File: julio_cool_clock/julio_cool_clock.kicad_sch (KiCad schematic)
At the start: 19 parts, among them J1 PJ-102AH, J2 Conn_01x06, Y1 Crystal_16MHz

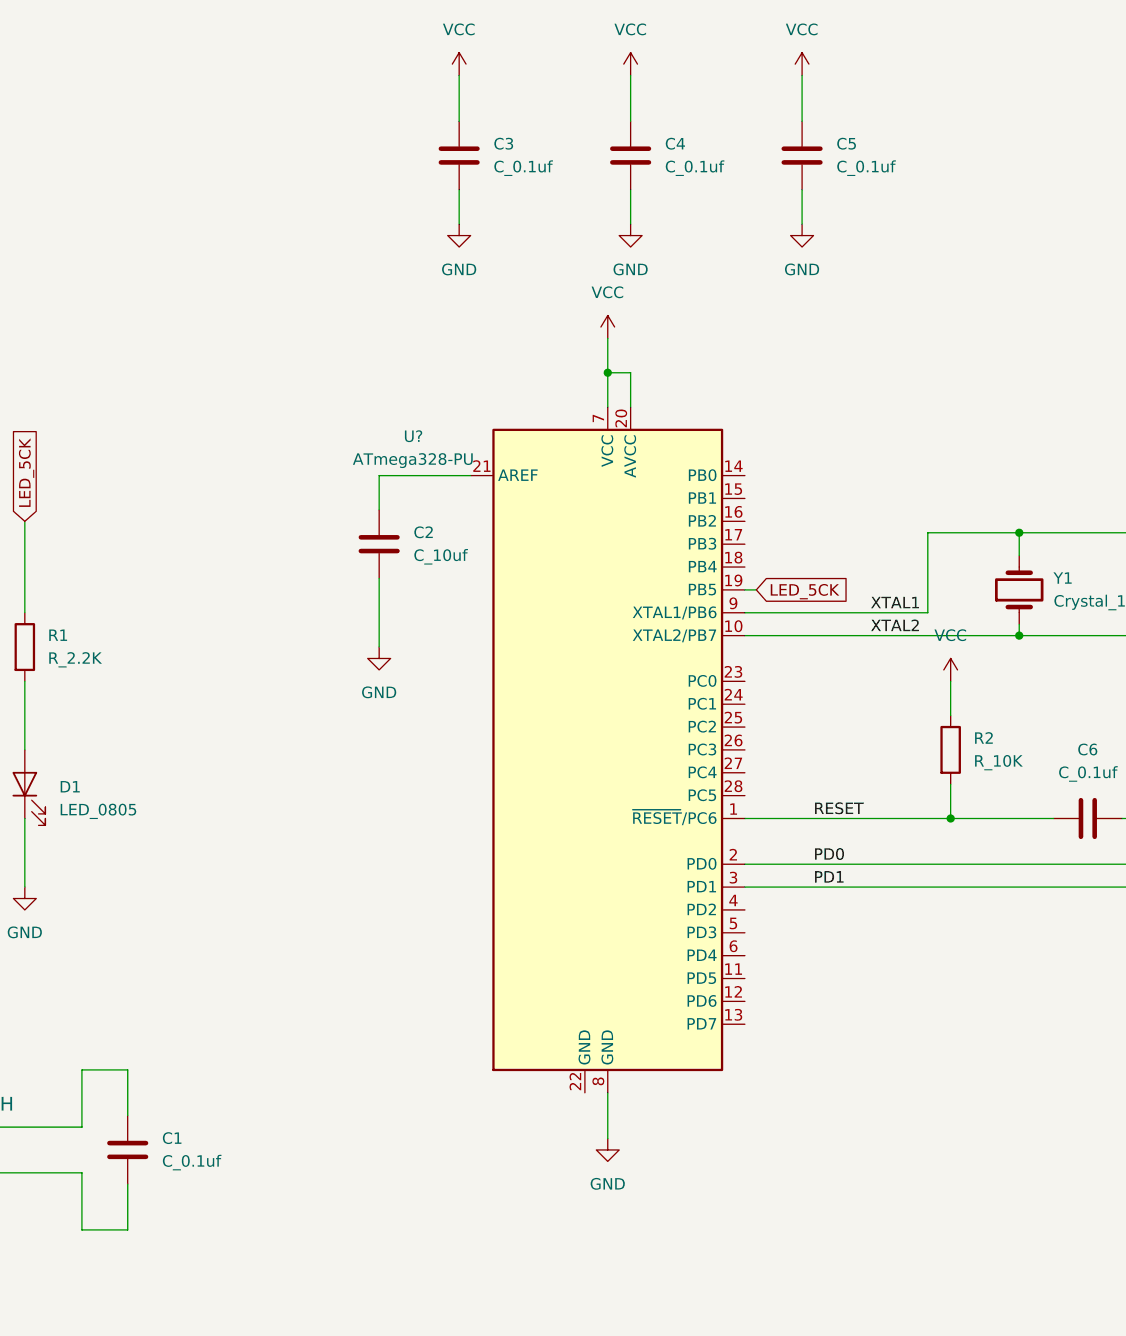
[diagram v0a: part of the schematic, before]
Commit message: Design Commit 1.1
Adjusted the starting schematic with 10uF capacitors in place of the polar capacitors in the lecture slide.
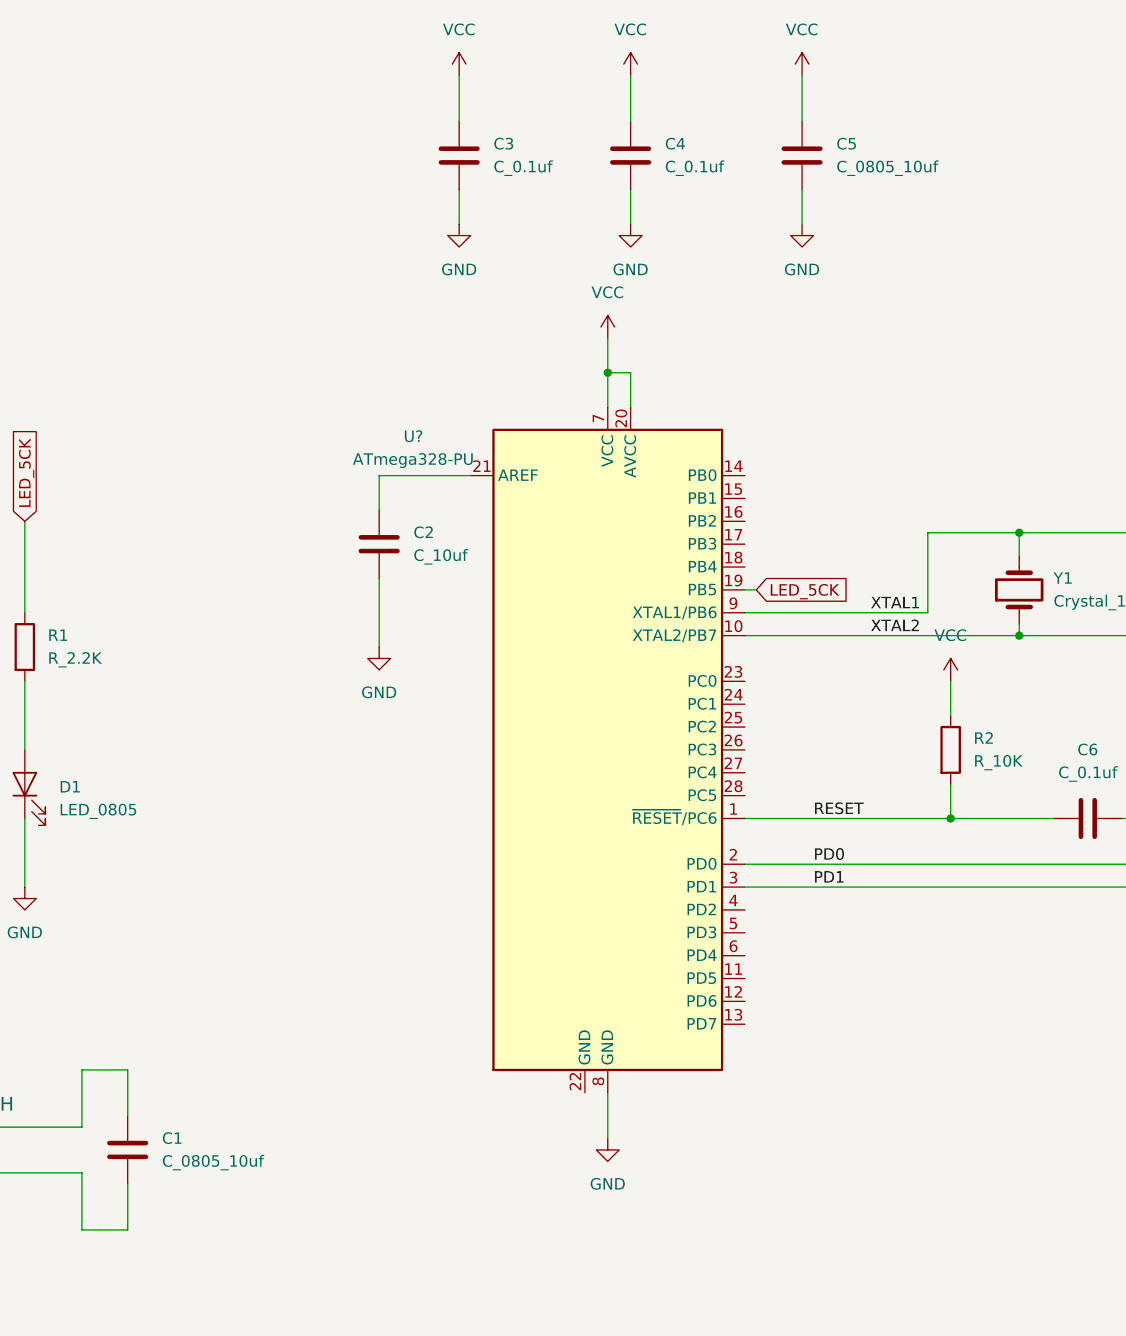
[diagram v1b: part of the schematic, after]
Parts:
- removed C1, C5: C_0.1uf, footprints:C_0805_2012Metric, symbol HPS:C_0805_0.1uf
- added C1, C5: C_0805_10uf, footprints:C_0805_2012Metric, symbol HPS:C_0805_10uf
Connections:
- net GND: now also C5.2
- net VCC: now also C5.1
- net at J1.1 (POLE): now also C1.1
- net at J1.2 (OUT): now also C1.2
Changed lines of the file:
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@@
+    (pin "2")
+  )
+  (symbol (lib_id "HPS:C_0805_10uf") (at 90.17 138.43 0) (unit 1)
+    (in_bom yes) (on_board yes) (fields_autoplaced)
+    (property "Reference" "C1" (id 0) (at 93.98 137.1599 0)
+      (effects (font (size 1.27 1.27)) (justify left))
+    )
+    (property "Value" "C_0805_10uf" (id 1) (at 93.98 139.6999 0)
+      (effects (font (size 1.27 1.27)) (justify left))
+    )
+    (property "Footprint" "footprints:C_0805_2012Metric" (id 2) (at 91.1352 142.24 0)
+      (effects (font (size 1.27 1.27)) hide)
+    )
+    (property "Datasheet" "https://search.murata.co.jp/Ceramy/image/img/A01X/G101/ENG/GRM21BR61E106KA73-01.pdf" (id 3) (at 90.805 135.89 0)
+      (effects (font (size 1.27 1.27)) hide)
+    )
+    (property "MFG" "Murata Electronics" (id 4) (at 90.17 144.78 0)
+      (effects (font (size 1.27 1.27)) hide)
+    )
+    (property "MPN" "GRM21BR61E106KA73L" (id 5) (at 90.17 147.32 0)
+      (effects (font (size 1.27 1.27)) hide)
+    )
+    (property "Digikey PN" "490-5523-1-ND" (id 6) (at 90.17 152.4 0)
+      (effects (font (size 1.27 1.27)) hide)
+    )
+    (property "Mouser PN" "N/A" (id 7) (at 90.17 154.94 0)
+      (effects (font (size 1.27 1.27)) hide)
+    )
+    (property "Voltage" "N/A" (id 8) (at 90.17 157.48 0)
+      (effects (font (size 1.27 1.27)) hide)
+    )
+    (property "Dielectric" "N/A" (id 9) (at 90.17 157.48 0)
+      (effects (font (size 1.27 1.27)) hide)
+    )
+    (property "Tolerance" "N/A" (id 10) (at 90.17 157.48 0)
+      (effects (font (size 1.27 1.27)) hide)
+    )
+    (pin "1")
     (pin "2")
   )
@@
     )
     (pin "1")
-  )
-  (symbol (lib_id "HPS:C_0805_0.1uf") (at 90.17 138.43 0) (unit 1)
-    (in_bom yes) (on_board yes) (fields_autoplaced)
-    (property "Reference" "C1" (id 0) (at 93.98 137.1599 0)
-      (effects (font (size 1.27 1.27)) (justify left))
-    )
-    (property "Value" "C_0.1uf" (id 1) (at 93.98 139.6999 0)
-      (effects (font (size 1.27 1.27)) (justify left))
-    )
-    (property "Footprint" "footprints:C_0805_2012Metric" (id 2) (at 91.1352 142.24 0)
-      (effects (font (size 1.27 1.27)) hide)
-    )
-    (property "Datasheet" "https://datasheets.avx.com/X7RDielectric.pdf" (id 3) (at 90.805 135.89 0)
-      (effects (font (size 1.27 1.27)) hide)
-    )
-    (property "MFG" "AVX Corporation" (id 4) (at 90.17 144.78 0)
-      (effects (font (size 1.27 1.27)) hide)
-    )
-    (property "MPN" "08055C104KAT2A" (id 5) (at 90.17 147.32 0)
-      (effects (font (size 1.27 1.27)) hide)
-    )
-    (property "Digikey PN" "478-1395-1-ND" (id 6) (at 90.17 152.4 0)
-      (effects (font (size 1.27 1.27)) hide)
-    )
-    (property "Mouser PN" "N/A" (id 7) (at 90.17 154.94 0)
-      (effects (font (size 1.27 1.27)) hide)
-    )
-    (property "Voltage" "N/A" (id 8) (at 90.17 157.48 0)
-      (effects (font (size 1.27 1.27)) hide)
-    )
-    (property "Dielectric" "N/A" (id 9) (at 90.17 157.48 0)
-      (effects (font (size 1.27 1.27)) hide)
-    )
-    (property "Tolerance" "N/A" (id 10) (at 90.17 157.48 0)
-      (effects (font (size 1.27 1.27)) hide)
-    )
-    (pin "1")
-    (pin "2")
   )
   (symbol (lib_id "HPS:VCC") (at 165.1 19.05 0) (unit 1)
@@
     (pin "2")
   )
-  (symbol (lib_id "HPS:C_0805_0.1uf") (at 165.1 27.94 0) (unit 1)
+  (symbol (lib_id "HPS:C_0805_10uf") (at 165.1 27.94 0) (unit 1)
     (in_bom yes) (on_board yes) (fields_autoplaced)
     (property "Reference" "C5" (id 0) (at 168.91 26.6699 0)
       (effects (font (size 1.27 1.27)) (justify left))
     )
-    (property "Value" "C_0.1uf" (id 1) (at 168.91 29.2099 0)
+    (property "Value" "C_0805_10uf" (id 1) (at 168.91 29.2099 0)
       (effects (font (size 1.27 1.27)) (justify left))
     )
@@
       (effects (font (size 1.27 1.27)) hide)
     )
-    (property "Datasheet" "https://datasheets.avx.com/X7RDielectric.pdf" (id 3) (at 165.735 25.4 0)
-      (effects (font (size 1.27 1.27)) hide)
-    )
-    (property "MFG" "AVX Corporation" (id 4) (at 165.1 34.29 0)
-      (effects (font (size 1.27 1.27)) hide)
-    )
-    (property "MPN" "08055C104KAT2A" (id 5) (at 165.1 36.83 0)
-      (effects (font (size 1.27 1.27)) hide)
-    )
-    (property "Digikey PN" "478-1395-1-ND" (id 6) (at 165.1 41.91 0)
+    (property "Datasheet" "https://search.murata.co.jp/Ceramy/image/img/A01X/G101/ENG/GRM21BR61E106KA73-01.pdf" (id 3) (at 165.735 25.4 0)
+      (effects (font (size 1.27 1.27)) hide)
+    )
+    (property "MFG" "Murata Electronics" (id 4) (at 165.1 34.29 0)
+      (effects (font (size 1.27 1.27)) hide)
+    )
+    (property "MPN" "GRM21BR61E106KA73L" (id 5) (at 165.1 36.83 0)
+      (effects (font (size 1.27 1.27)) hide)
+    )
+    (property "Digikey PN" "490-5523-1-ND" (id 6) (at 165.1 41.91 0)
       (effects (font (size 1.27 1.27)) hide)
     )
@@
       (reference "#PWR?") (unit 1) (value "GND") (footprint "")
     )
-    (path "/862e7416-362f-490f-9b26-7a6c1e75c0c9"
-      (reference "C1") (unit 1) (value "C_0.1uf") (footprint "footprints:C_0805_2012Metric")
+    (path "/6f97759c-1ad8-4f0e-a04e-d2e50a497ce6"
+      (reference "C1") (unit 1) (value "C_0805_10uf") (footprint "footprints:C_0805_2012Metric")
     )
     (path "/d1f31220-e097-488d-9540-ed62728793d1"
@@
       (reference "C4") (unit 1) (value "C_0.1uf") (footprint "footprints:C_0805_2012Metric")
     )
-    (path "/e1700882-ee6c-4685-9457-9c368506616a"
-      (reference "C5") (unit 1) (value "C_0.1uf") (footprint "footprints:C_0805_2012Metric")
+    (path "/efddba53-3b77-46b4-8321-0aff9be2da48"
+      (reference "C5") (unit 1) (value "C_0805_10uf") (footprint "footprints:C_0805_2012Metric")
     )
     (path "/2f4099bf-4d54-4041-920b-635ae3bcc86c"

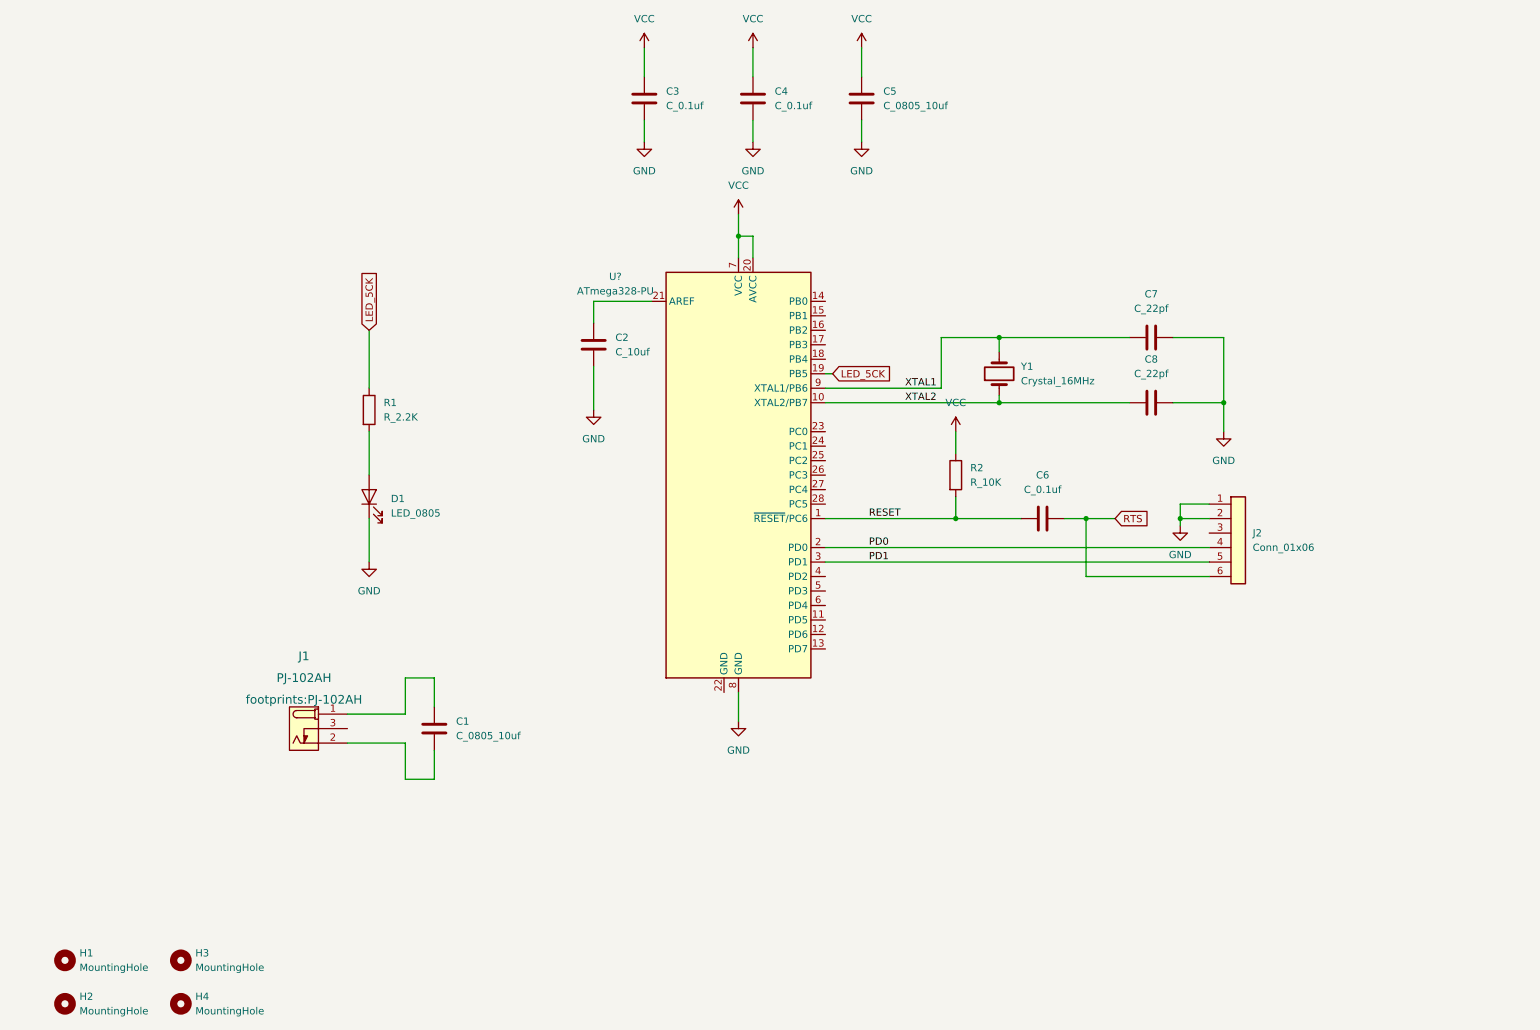
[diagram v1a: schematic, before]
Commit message: Design Commit 2
In this commit, I adjusted the MCU schematic section and added the power input portion.
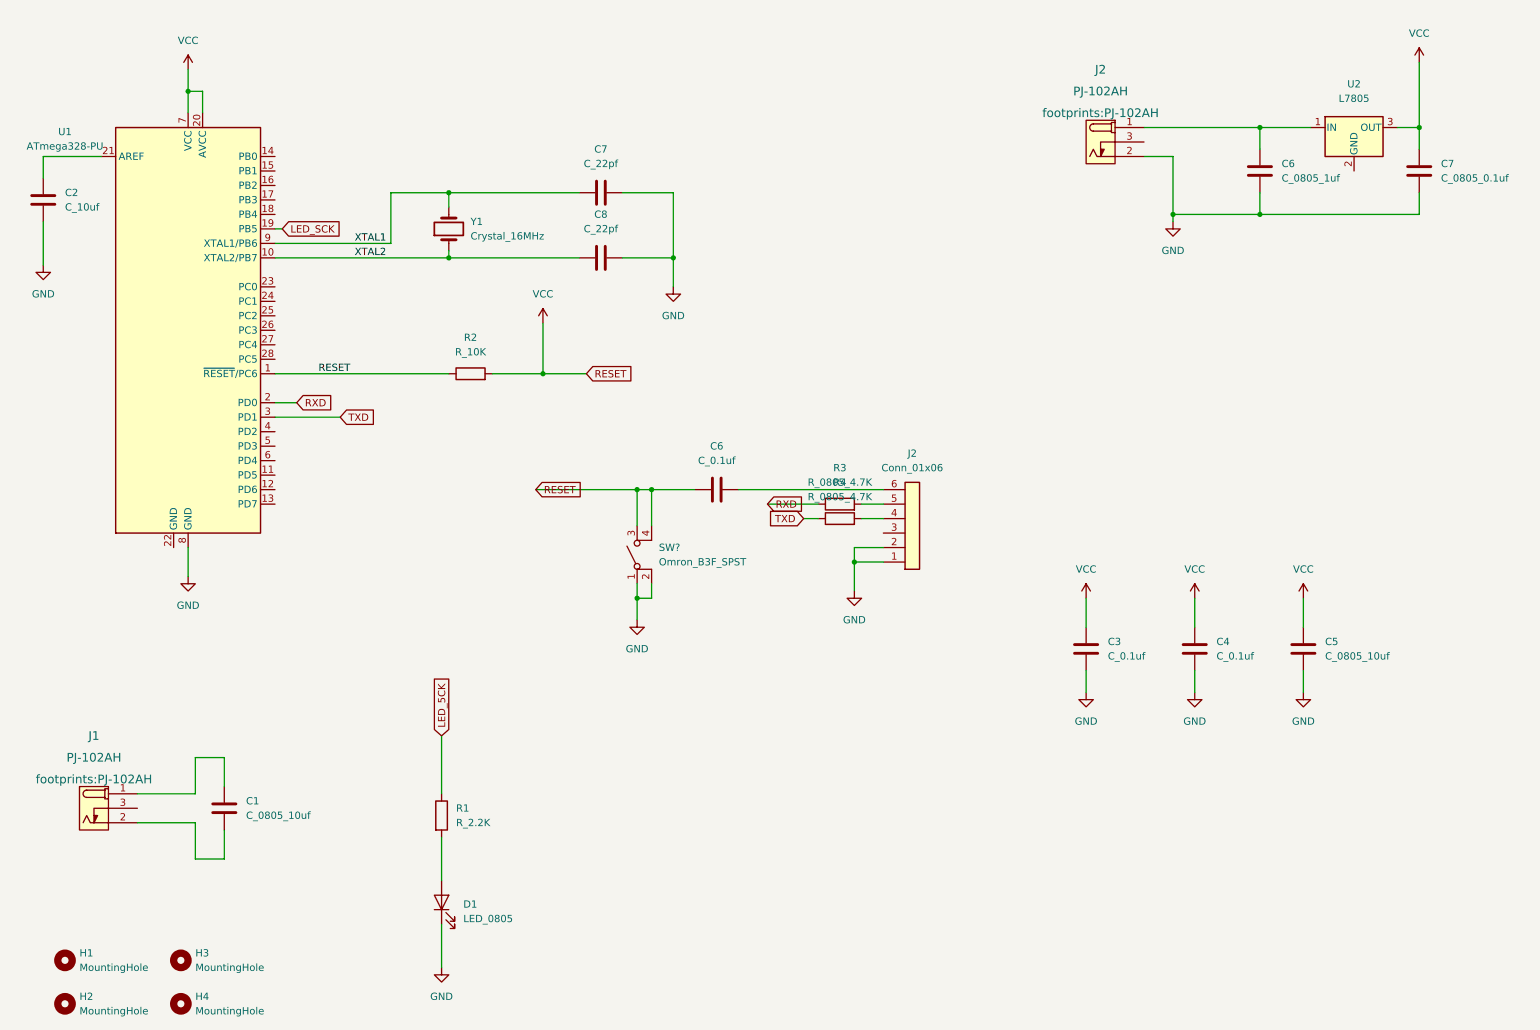
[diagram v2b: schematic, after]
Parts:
- added C6: C_0805_1uf, footprints:C_0805_2012Metric, symbol HPS:C_0805_1uf
- added C7: C_0805_0.1uf, footprints:C_0805_2012Metric, symbol HPS:C_0805_0.1uf
- added J2: PJ-102AH, footprints:PJ-102AH, symbol HPS:PJ-102AH
- added R3, R4: R_0805_4.7K, footprints:R_0805_2012Metric, symbol HPS:R_0805_4.7K
- added SW?: Omron_B3F_SPST, footprints:SW_SPST_Omron_B3FS-100xP, symbol HPS:Omron_B3F_SPST
- added U2: L7805, symbol HPS:L7805
- gave numbers to parts that had none: 1
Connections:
- net RESET is gone; now on net VCC: C6.1, R2.2, U1.1 (~{RESET}/PC6)
- net GND: now also C6.2, C7.2, J2.2 (OUT), SW?.1 (A), SW?.2 (A)
- net LED_5CK: no longer U1.19 (PB5)
- net VCC: now also C7.1, SW?.3 (B), SW?.4 (B), U2.3 (OUT)
- net PD0: no longer names the net of J2.4 (Pin_4)
- net PD0: now also R4.2; no longer U1.2 (PD0)
- net PD1: no longer names the net of J2.5 (Pin_5)
- net PD1: now also R3.2; no longer U1.3 (PD1)
- net RTS: no longer names the net of C6.2, J2.6 (Pin_6)
- new net: C6.1, J2.1 (POLE), U2.1 (IN)
- new net LED_SCK: U1.19 (PB5)
- new net RXD: R3.1, U1.2 (PD0)
- new net TXD: R4.1, U1.3 (PD1)
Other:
- moved on the sheet: C1, C2, C3, C4, C5, C6, C7, C8, D1, J1, J2, R1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
